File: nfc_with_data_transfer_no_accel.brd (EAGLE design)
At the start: 15.4 x 25.1 mm, 8 parts

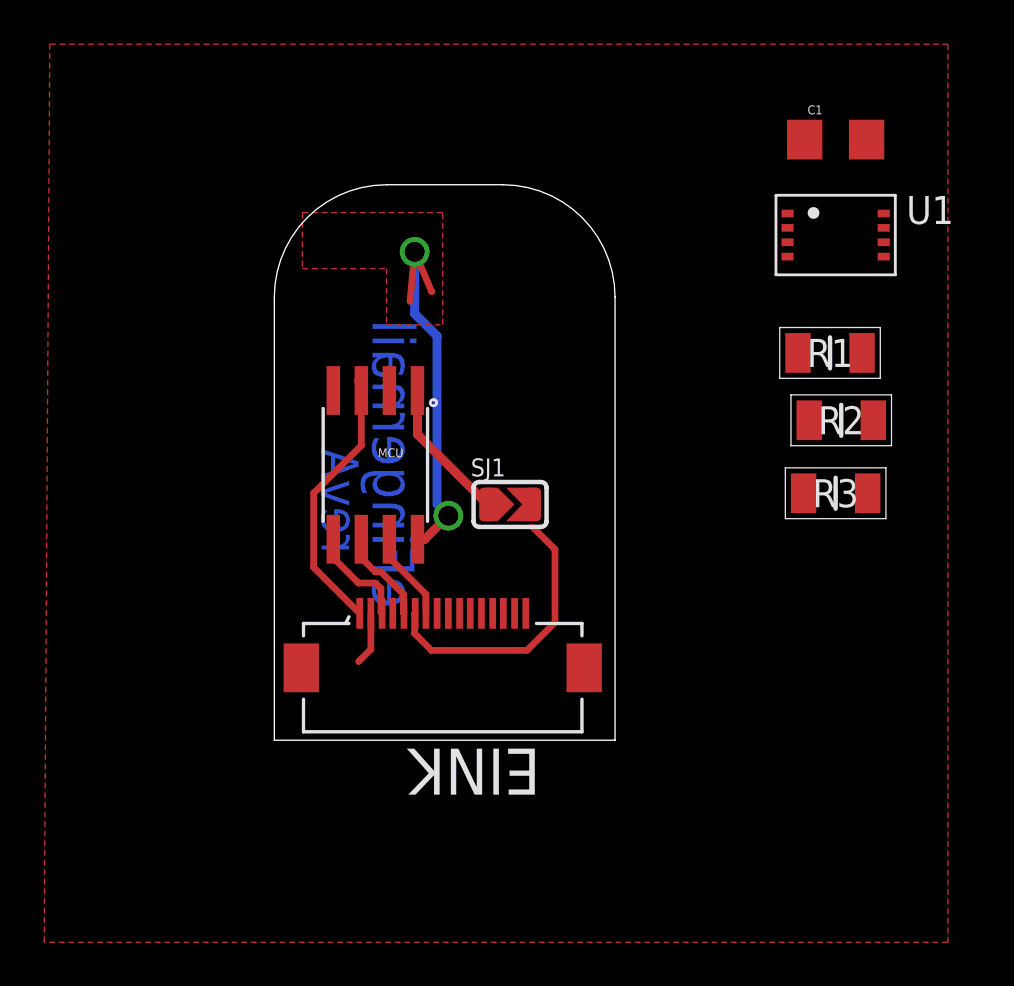
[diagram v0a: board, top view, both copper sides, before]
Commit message: Updated board (with traces and embedded coil)
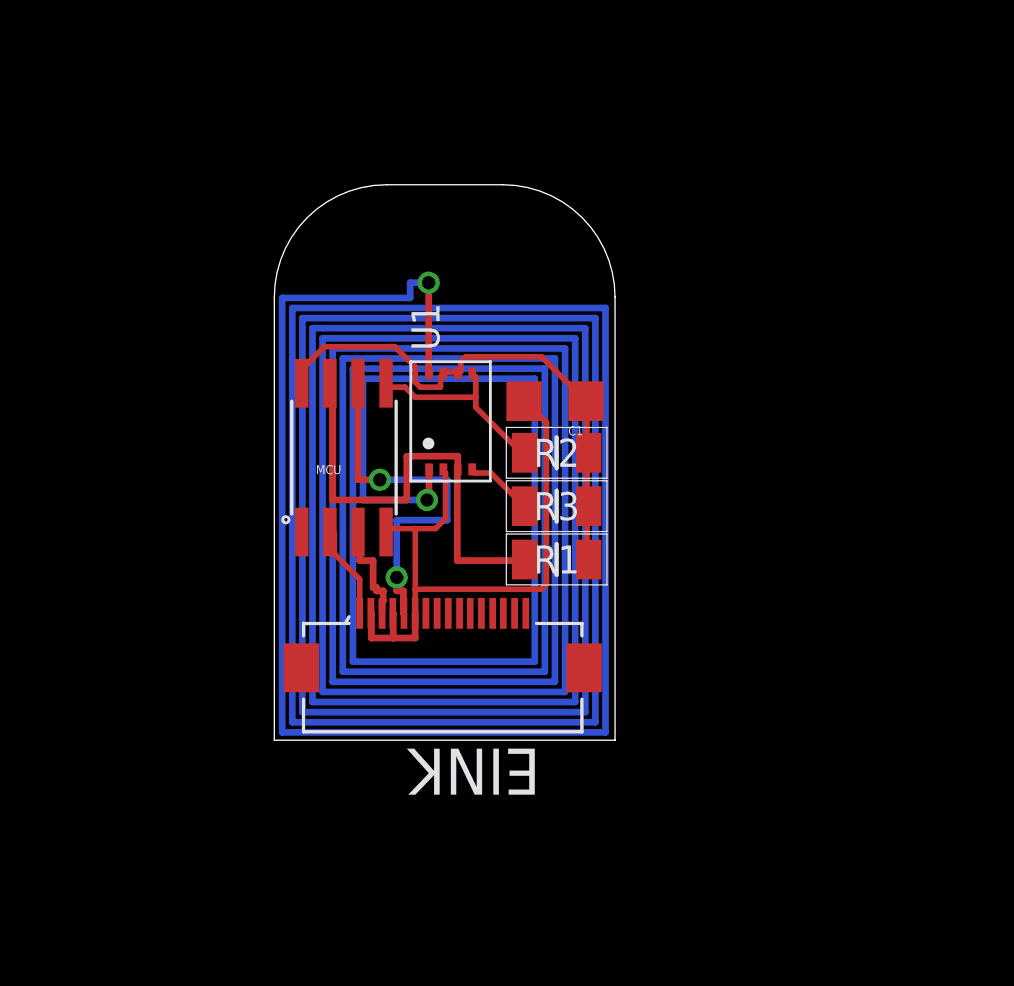
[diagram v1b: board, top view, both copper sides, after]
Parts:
- removed SJ1: (no value), microbuilder:SOLDERJUMPER_ARROW_NOPASTE
- moved U1 19.4 mm to (10.5, 14.7), turned to 90 degrees
- moved C1 17.4 mm to (15.2, 15.6), turned to 180 degrees
- moved R1 15.5 mm to (15.3, 8.43)
- moved R2 13.0 mm to (15.3, 13.3)
- moved R3 12.6 mm to (15.3, 10.8)
- moved MCU 1.47 mm to (5.69, 13.1), turned to 0 degrees
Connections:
- net N$2 renamed FD
- removed net DOT2: EINK.4
- removed net DOT4: EINK.6
- removed net GND: C1.2, EINK.2, MCU.4, U1.2
- removed net N$1: MCU.1, SJ1.1
- new net VSS: C1.2, EINK.2, EINK.4, EINK.6, MCU.4, U1.2
- net CLOCK: now also R1.1
- net DATA: now also R2.1
- net DOT1: now also MCU.3; no longer MCU.2
- net DOT5: no longer SJ1.2
- net RST: now also MCU.2; no longer MCU.3
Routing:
- net COIL: track 0.00 -> 460.2 mm, vias 0 -> 2
- net VSS: track 0.00 -> 29.2 mm
- net CLOCK: track 0.00 -> 20.9 mm
- net DOT3: track 3.46 -> 17.1 mm, vias 0 -> 2
- net DOT4: track 12.9 -> 0.00 mm
- net DATA: track 0.00 -> 9.00 mm
- net RST: track 13.0 -> 4.30 mm
- net 2.8V: track 18.6 -> 25.2 mm, vias 2 -> 0
- net N$1: track 6.47 -> 0.00 mm
- net DOT5: track 3.20 -> 0.00 mm
- net FD: track 0.00 -> 3.06 mm
- net GND: track 2.42 -> 0.00 mm
- net DOT1: track 3.88 -> 4.88 mm
- removed copper zone on layer 1, net 2.8V
- removed copper zone on layer 1, net GND
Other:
- board text removed: "eFingernail"
- board text removed: "revA"
